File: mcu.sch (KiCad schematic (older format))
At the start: 47 parts, among them J2 WE-61300511121, J3 WE-61301011121, J4 Samtec-FTSH-105-01-F-DV-K-TR, U2 RaltronElectronics-RT3215-32.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, U3 Espressif_ESP32-D0WDQ6-V3

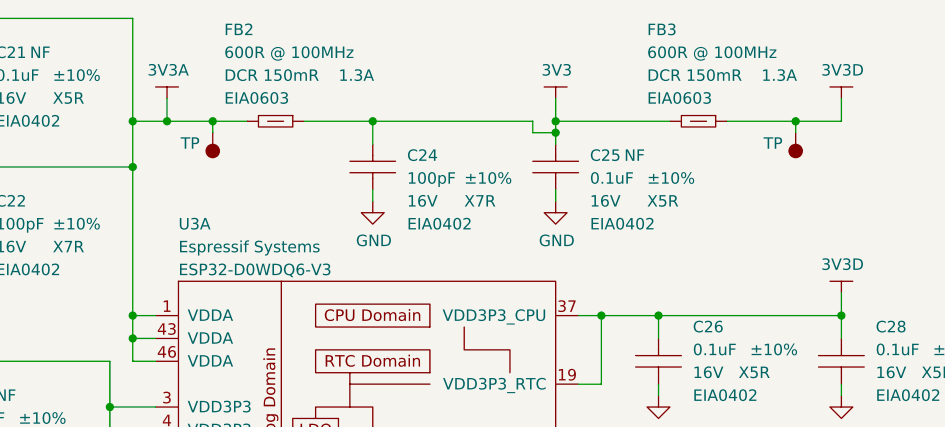
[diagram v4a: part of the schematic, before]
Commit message: Update power symbols after change to pin names; annotate.
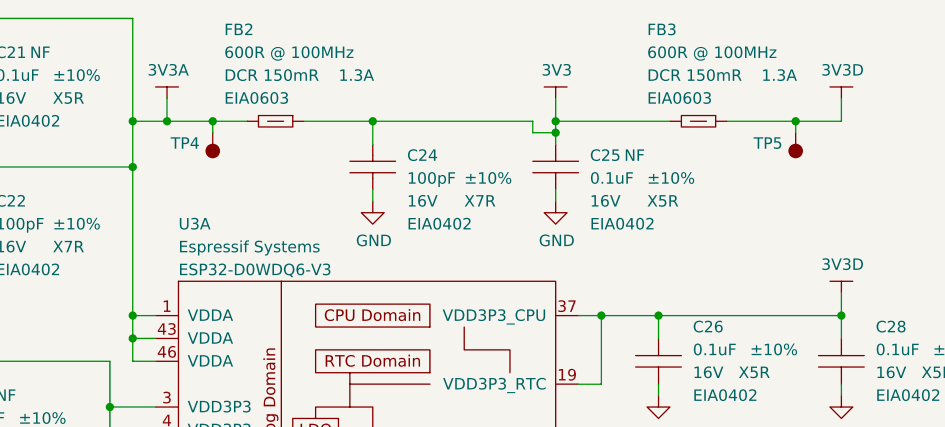
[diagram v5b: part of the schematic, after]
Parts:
- renumbered TP to TP4, TP to TP5
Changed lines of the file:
@@
 U 1 1 605023F2
 P 9250 1000
+AR Path="/605023F2" Ref="#PWR0126"  Part="1"
+AR Path="/60330427/605023F2" Ref="#PWR0126"  Part="1"
 F 0 "#PWR0126" H 9400 950 50  0001 C CNN
 F 1 "3V3" H 9255 1123 50  0000 C CNN
@@
 	3800 2150 3550 2150
 $Comp
-L gz_Test-Points:Test-Point-SMT TP
+L gz_Test-Points:Test-Point-SMT TP4
 U 1 1 60505B45
 P 7750 1150
-F 0 "TP" H 7807 1197 50  0000 L CNN
+F 0 "TP4" H 7807 1197 50  0000 L CNN
 F 1 "Test-Point-SMT" H 8050 1500 50  0001 L CNN
 F 2 "footprints_generic:TestPoint-SMT_C100" H 8050 1400 50  0001 L CNN
@@
 U 1 1 605A485C
 P 7550 1000
+AR Path="/605A485C" Ref="#PWR0134"  Part="1"
+AR Path="/60330427/605A485C" Ref="#PWR0134"  Part="1"
 F 0 "#PWR0134" H 7700 950 50  0001 C CNN
 F 1 "3V3A" H 7555 1123 50  0000 C CNN
@@
 U 1 1 605A8213
 P 3800 2050
+AR Path="/605A8213" Ref="#PWR0135"  Part="1"
+AR Path="/60330427/605A8213" Ref="#PWR0135"  Part="1"
 F 0 "#PWR0135" H 3950 2000 50  0001 C CNN
 F 1 "3V3A" H 3805 2173 50  0000 C CNN
@@
 U 1 1 605D3C18
 P 10500 1000
+AR Path="/605D3C18" Ref="#PWR0136"  Part="1"
+AR Path="/60330427/605D3C18" Ref="#PWR0136"  Part="1"
 F 0 "#PWR0136" H 10650 950 50  0001 C CNN
 F 1 "3V3D" H 10505 1123 50  0000 C CNN
@@
 U 1 1 605D7425
 P 10500 1850
+AR Path="/605D7425" Ref="#PWR0137"  Part="1"
+AR Path="/60330427/605D7425" Ref="#PWR0137"  Part="1"
 F 0 "#PWR0137" H 10650 1800 50  0001 C CNN
 F 1 "3V3D" H 10505 1973 50  0000 C CNN
@@
 Connection ~ 10500 1950
 $Comp
-L gz_Test-Points:Test-Point-SMT TP
+L gz_Test-Points:Test-Point-SMT TP5
 U 1 1 605DAA4E
 P 10300 1150
-F 0 "TP" H 10357 1197 50  0000 L CNN
+F 0 "TP5" H 10357 1197 50  0000 L CNN
 F 1 "Test-Point-SMT" H 10600 1500 50  0001 L CNN
 F 2 "footprints_generic:TestPoint-SMT_C100" H 10600 1400 50  0001 L CNN
@@
 U 1 1 607B6F1E
 P 950 1200
+AR Path="/607B6F1E" Ref="#PWR0148"  Part="1"
+AR Path="/60330427/607B6F1E" Ref="#PWR0148"  Part="1"
 F 0 "#PWR0148" H 1100 1150 50  0001 C CNN
 F 1 "3V3" H 955 1323 50  0000 C CNN
